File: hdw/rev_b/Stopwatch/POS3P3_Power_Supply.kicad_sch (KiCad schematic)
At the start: 17 parts, among them U301 TPS62130A

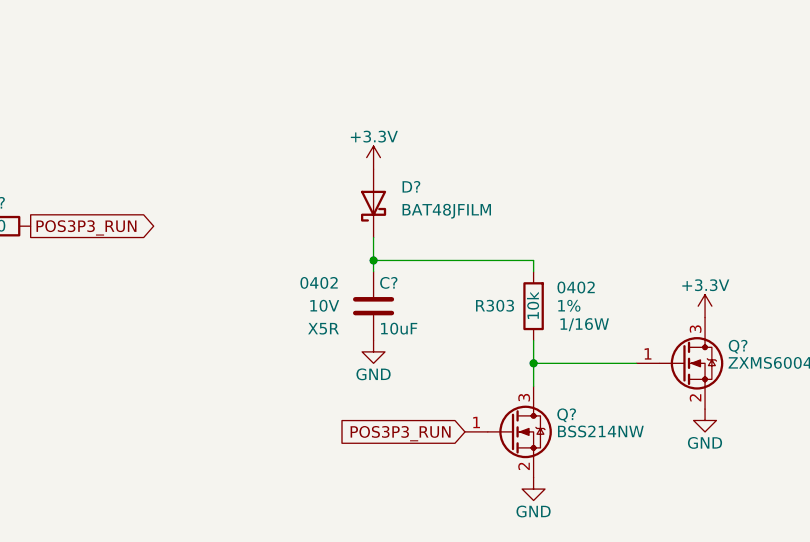
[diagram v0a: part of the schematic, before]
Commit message: ported rev b to kicad 8
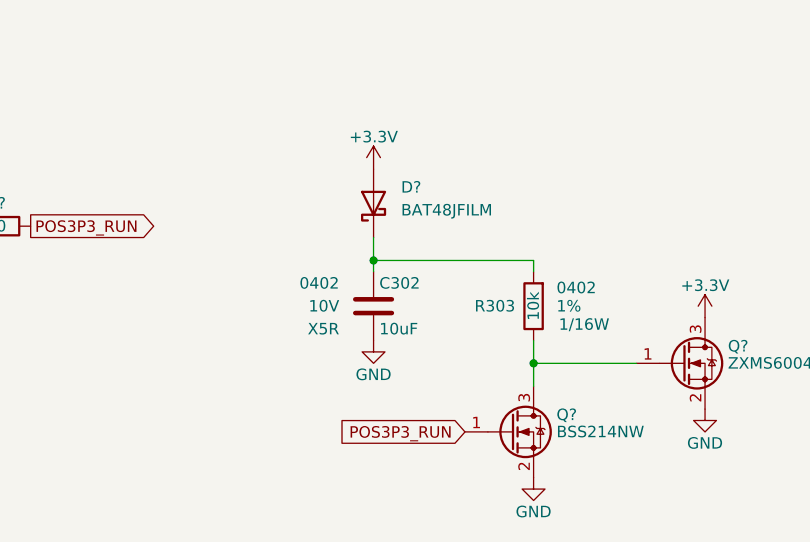
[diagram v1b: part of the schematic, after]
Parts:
- gave numbers to parts that had none: 1
